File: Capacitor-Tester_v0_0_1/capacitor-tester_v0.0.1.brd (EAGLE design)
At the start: 100 x 80 mm, 32 parts, among them IC1 AD8531ARZ, IC2 MC34063EBD-TR, IC3 DAC6571IDBVT, IC5 AD8397ARDZ, J1 USB4125-GF-A-0190_REVA2, J2 DS1044-140G, J4 250-103, U1 AD5933, Y1 LFSPXO018034

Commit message: IN PROGRESS - arranging elements
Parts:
- added C3, C7: 100n, custom_library:C0603
- R15: value 5k-1% -> 10k-1%
- moved R15 345.0 mm to (59.6, 35.5), turned to 90 degrees
- moved L1 342.9 mm to (24.4, 26.1), flipped to the bottom, turned to 270 degrees
- moved R16 336.6 mm to (60.8, 22.1), turned to 270 degrees
- moved R6 330.2 mm to (56.8, 22.1), turned to 90 degrees
- moved R4 329.6 mm to (8.75, 33.1), turned to 270 degrees
- moved R5 329.1 mm to (58.8, 22.1), turned to 270 degrees
- moved R2 328.7 mm to (10.8, 32.9), turned to 90 degrees
- moved D2 319.7 mm to (7.25, 19.5), turned to 90 degrees
- moved IC1 319.1 mm to (8.00, 26.6), turned to 90 degrees
- moved IC5 318.6 mm to (59.0, 28.8), turned to 90 degrees
- moved C8 312.0 mm to (47.6, 32.2), turned to 270 degrees
- moved IC3 295.4 mm to (46.6, 38.1), turned to 90 degrees
- moved C6 247.8 mm to (16.5, 34.8), flipped to the bottom
- moved C5 244.0 mm to (36.0, 38.8), flipped to the bottom, turned to 90 degrees
- moved J4 242.9 mm to (15.8, 5.40)
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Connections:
- net +12V: now also C3.1; no longer D2.1
- net +5V: now also C7.1, D2.1
- net GND: now also C3.2, C7.2
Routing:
- net +5V: track 0.00 -> 128.6 mm, vias 0 -> 3
- net Z_OUT: track 0.00 -> 79.7 mm
- net SDA: track 0.00 -> 66.4 mm, vias 0 -> 1
- net +12V: track 0.00 -> 65.5 mm, vias 0 -> 2
- net SCL: track 0.00 -> 64.2 mm, vias 0 -> 1
- net VIN: track 0.00 -> 48.6 mm
- net UZA_OUT: track 0.00 -> 39.2 mm
- net VOUT: track 0.00 -> 38.4 mm
- net MCLK: track 0.00 -> 24.4 mm
- net FUNC_GEN: track 0.00 -> 20.4 mm
- net DAC_OUT: track 0.00 -> 18.9 mm, vias 0 -> 2
- net N$13: track 0.00 -> 17.1 mm
- net N$11: track 0.00 -> 15.7 mm
- net UZB_OUT: track 0.00 -> 11.7 mm
- net N$5: track 0.00 -> 10.3 mm
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- added copper zone on layer 1, net GND
- added copper zone on layer 16, net GND
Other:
- board size 100 x 80 mm -> 67 x 45 mm

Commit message: IN PROGRESS - arranging elements
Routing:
- net +5V: track 128.6 -> 0.00 mm
- net Z_OUT: track 79.7 -> 0.00 mm
- net SDA: track 66.4 -> 0.00 mm
- net +12V: track 65.5 -> 0.00 mm
- net SCL: track 64.2 -> 0.00 mm
- net VIN: track 48.6 -> 0.00 mm
- net UZA_OUT: track 39.2 -> 0.00 mm
- net VOUT: track 38.4 -> 0.00 mm
- net MCLK: track 24.4 -> 0.00 mm
- net FUNC_GEN: track 20.4 -> 0.00 mm
- net DAC_OUT: track 18.9 -> 0.00 mm
- net N$13: track 17.1 -> 0.00 mm
- net N$11: track 15.7 -> 0.00 mm
- net UZB_OUT: track 11.7 -> 0.00 mm
- net N$5: track 10.3 -> 0.00 mm
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
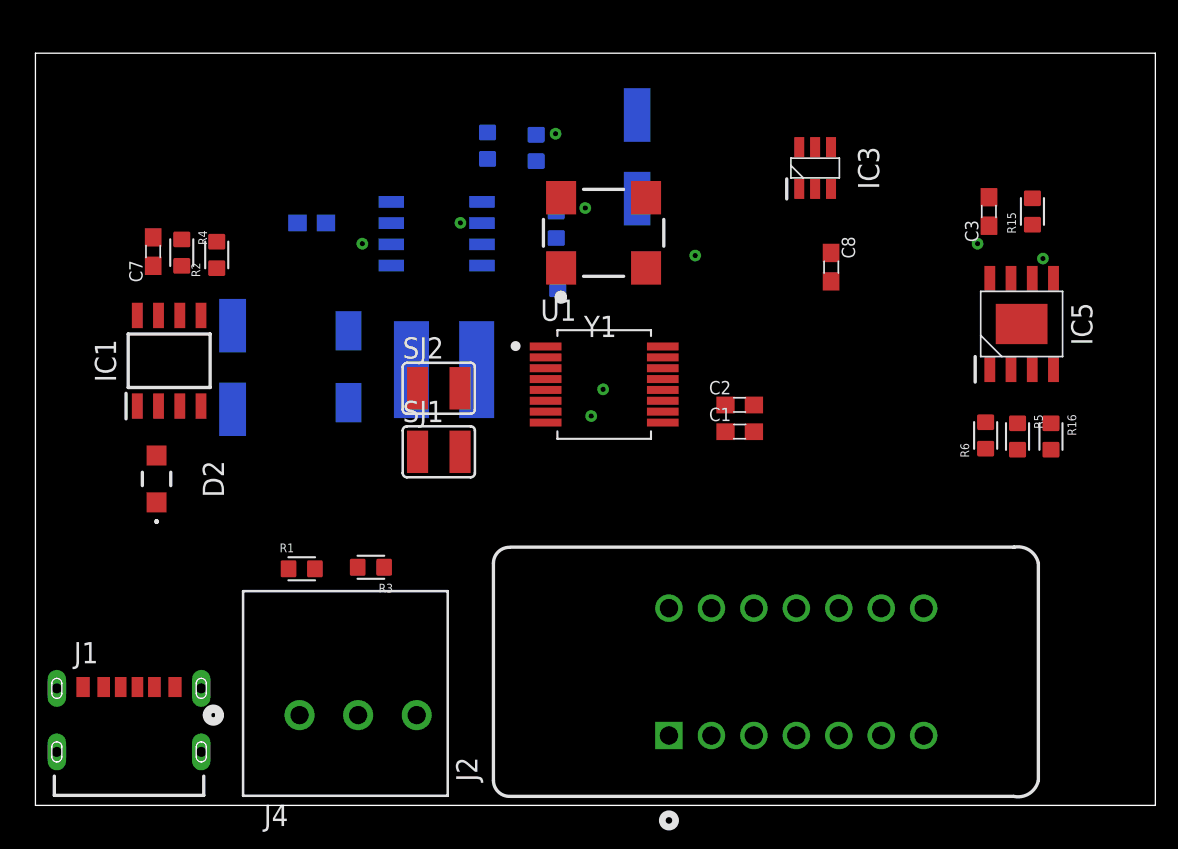
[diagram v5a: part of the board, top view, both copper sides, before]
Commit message: v0.0.1 - Routed traces
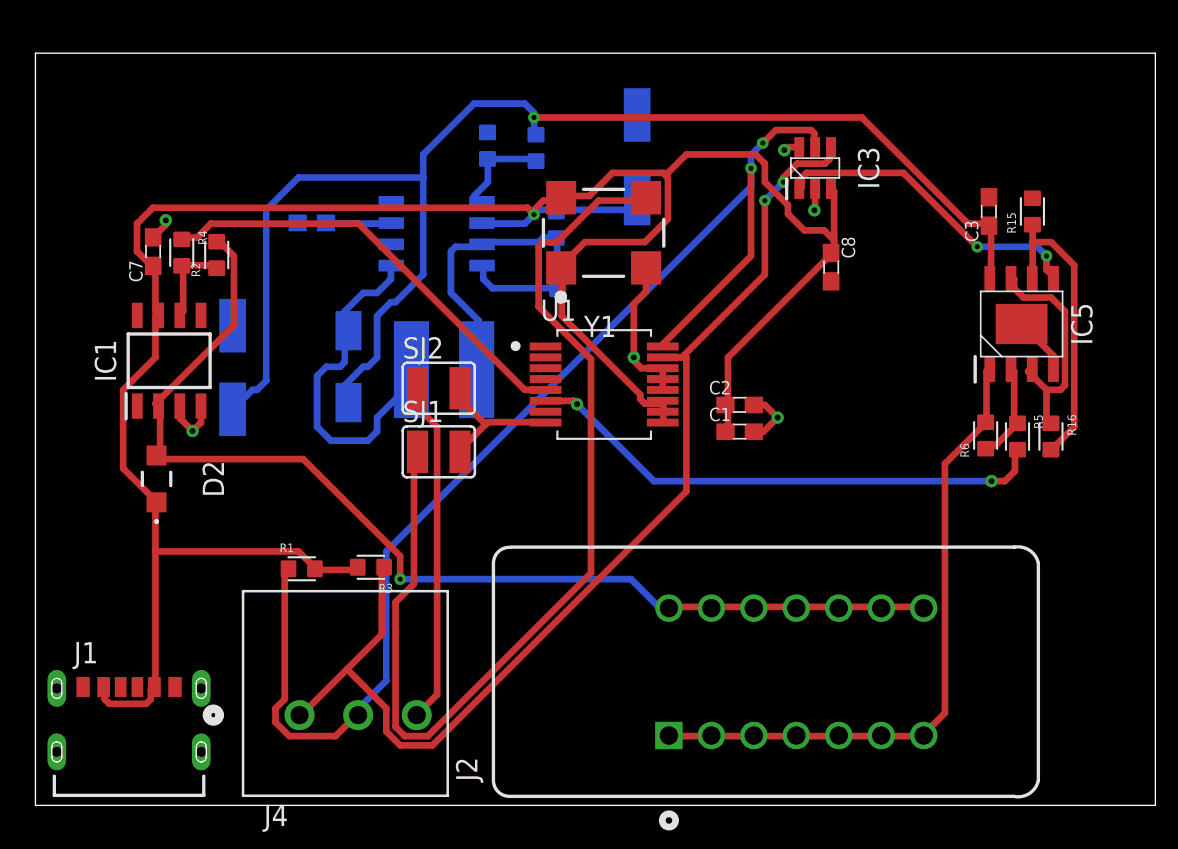
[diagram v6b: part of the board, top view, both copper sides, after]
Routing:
- net +5V: track 0.00 -> 144.9 mm, vias 3 -> 1
- net +12V: track 0.00 -> 82.9 mm, vias 2 -> 1
- net SCL: track 0.00 -> 76.8 mm, vias 1 -> 2
- net SDA: track 0.00 -> 66.9 mm, vias 1 -> 2
- net Z_OUT: track 0.00 -> 66.3 mm, vias 0 -> 1
- net MCLK: track 0.00 -> 61.5 mm
- net UZA_OUT: track 0.00 -> 38.9 mm
- net VOUT: track 0.00 -> 31.7 mm, vias 0 -> 2
- net VIN: track 0.00 -> 26.3 mm
- net GND: track 0.00 -> 23.2 mm, vias 0 -> 6
- net N$5: track 0.00 -> 21.4 mm
- net FUNC_GEN: track 0.00 -> 20.5 mm
- net DAC_OUT: track 0.00 -> 19.1 mm
- net N$13: track 0.00 -> 18.1 mm
- net N$11: track 0.00 -> 15.9 mm
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
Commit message: v0.0.1 - CMD renumber + tnames + bnames
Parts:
- removed IC5: AD8397ARDZ, AD8397ARDZ:SOIC127P600X175-9N
- removed J4: 250-103, custom_library:CONN3_250-103_WAG
- removed R15, R16: 10k-1%, custom_library:R0603
- added IC4: MC34063EBD-TR, MC34063EBD-TR:SOIC127P600X175-8N
- added J3: USB4125-GF-A-0190_REVA2, USB-C-6Pin:GCT_USB4125-GF-A-0190_REVA2
- added R7, R8: DNP-4k7-1%, custom_library:R0603
- C2: value 10u -> 100n
- C3: value 100n -> 10u
- C4: value 270u / 16V -> 10u; device EEEFKC271XSP:EEE0JA331XP -> custom_library:C0603
- C5: value 270u / 16V -> 100n; device EEEFKC271XSP:EEE0JA331XP -> custom_library:C0603
- C6: value 560p -> 270u / 16V; device custom_library:C0603 -> EEEFKC271XSP:EEE0JA331XP
- C7: value 100n -> 560p
- C8: value 10u -> 270u / 16V; device custom_library:C0603 -> EEEFKC271XSP:EEE0JA331XP
- D1: value SS14 -> PMEG6020ER,115; device SS14:DIOM5227X270N -> PMEG6020ER_115:PMEG6020ER115
- D2: value PMEG6020ER,115 -> SS14; device PMEG6020ER_115:PMEG6020ER115 -> SS14:DIOM5227X270N
- IC1: value AD8531ARZ -> DAC6571IDBVT; device AD8531ARZ:SOIC127P600X175-8N -> DAC6571IDBVT:SOT95P280X145-6N
- IC2: value MC34063EBD-TR -> AD8397ARDZ; device MC34063EBD-TR:SOIC127P600X175-8N -> AD8397ARDZ:SOIC127P600X175-9N
- IC3: value DAC6571IDBVT -> AD8531ARZ; device DAC6571IDBVT:SOT95P280X145-6N -> AD8531ARZ:SOIC127P600X175-8N
- J1: value USB4125-GF-A-0190_REVA2 -> DS1044-140G; device USB-C-6Pin:GCT_USB4125-GF-A-0190_REVA2 -> DS1044-140G:CONNFLY_DS1044-140G
- J2: value DS1044-140G -> 250-103; device DS1044-140G:CONNFLY_DS1044-140G -> custom_library:CONN3_250-103_WAG
- R1, R3: value DNP-4k7-1% -> 10k-1%
- R10: value 1k-1% -> R133-1%
- R11: value R133-1% -> 8k66-1%
- R12: value 180R-1% -> 1k-1%
- R2: value 10k-1% -> DNP-10k-1%
- R4: value DNP-10k-1% -> 1k-1%
- R6: value 1k-1% -> 10k-1%
- R9: value 8k66-1% -> 180R-1%
- moved R4 49.3 mm to (56.8, 22.1), turned to 90 degrees
- moved R1 48.7 mm to (59.6, 35.5), turned to 90 degrees
- moved IC1 40.3 mm to (46.6, 38.1)
- moved IC3 40.3 mm to (8.00, 26.6)
- moved J1 40.1 mm to (45.5, 7.99), turned to 90 degrees
- moved C2 36.3 mm to (7.05, 33.1), turned to 90 degrees
- moved IC2 35.4 mm to (59.0, 28.8), flipped to the top, turned to 90 degrees
- moved C4 30.4 mm to (42.1, 24.0), flipped to the top, turned to 0 degrees
- moved J2 29.8 mm to (15.8, 5.40), turned to 0 degrees
- moved R3 20.8 mm to (10.8, 32.9), turned to 90 degrees
- moved C1 19.9 mm to (57.0, 35.5), turned to 90 degrees
- moved C5 17.6 mm to (42.1, 22.4), flipped to the top, turned to 0 degrees
- moved C8 13.3 mm to (36.0, 38.8), flipped to the bottom, turned to 90 degrees
- moved D1 13.3 mm to (7.25, 19.5), flipped to the top
- moved D2 13.3 mm to (18.7, 26.2), flipped to the bottom
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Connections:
- net +12V: now also C1.1, C6.1, D2.1, IC2.8, R11.1; no longer C3.1, C4.1, D1.1, IC5.8, R9.1
- net +5V: now also C3.1, C4.1, D1.1, IC1.3, IC3.7, IC4.6, J3.A9, J3.B9, R10.1, R7.2, R8.2; no longer C1.1, C7.1, D2.1, IC1.7, IC2.6, IC3.3, J1.A9, J1.B9, R1.2, R11.1, R3.2
- net DAC_OUT: now also IC1.1, IC2.5; no longer IC3.1, IC5.5
- net FUNC_GEN: now also J2.3, SJ1.1; no longer J4.3, SJ2.1
- net GND: now also IC1.2, IC1.6, IC2.9, IC3.3, IC3.4, IC4.2, IC4.4, J3.A12, J3.B12, J3.S1, J3.S2, J3.S3, J3.S4, R1.2, R12.2; no longer IC1.3, IC1.4, IC2.2, IC3.2, IC3.6, IC5.4, IC5.9, J1.A12, J1.B12, J1.S1, J1.S2, J1.S3, J1.S4, R10.2, R15.2
- net MCLK: now also SJ2.1; no longer SJ1.1
- net N$1: now also IC3.6, R2.2, R3.1; no longer IC1.6, R2.1, R4.2
- net N$10: now also C7.1, IC4.3; no longer C6.1, IC2.3
- net N$11: now also IC4.7, R10.2, R9.2; no longer IC2.7, R11.2, R12.2
- net N$13: now also IC2.6, R1.1, R6.2; no longer IC5.6, R15.1, R16.2
- net N$4: now also IC2.2, R4.1; no longer IC5.2, R6.1
- net N$5: now also D2.2, IC4.1; no longer D1.2, IC2.1
- net N$7: now also IC4.5, R11.2, R12.1; no longer IC2.5, R10.1, R9.2
- net N$8: now also IC4.8, R9.1; no longer IC2.8, R12.1
- net SCL: now also IC1.5, J2.2, R8.1; no longer IC3.5, J4.2, R1.1
- net SDA: now also IC1.4, J2.1, R7.1; no longer IC3.4, J4.1, R3.1
- net UZA_OUT: now also IC2.1, J1.1, J1.2, J1.3, J1.4, J1.5, J1.6, J1.7, R4.2; no longer IC5.1, J2.1, J2.2, J2.3, J2.4, J2.5, J2.6, J2.7, R6.2
- net UZB_OUT: now also IC2.3, IC2.7, R6.1; no longer IC5.3, IC5.7, R16.1
- net VIN: now also R2.1; no longer R4.1
- net Z_OUT: now also D1.2, IC3.2, J1.10, J1.11, J1.12, J1.13, J1.14, J1.8, J1.9, R3.2; no longer D2.2, IC1.2, J2.10, J2.11, J2.12, J2.13, J2.14, J2.8, J2.9, R2.2
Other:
- board text added: "FUNC_GEN"
- board text added: "MCLK"

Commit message: v0.0.1 - Revert to commit b06d3d6
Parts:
- removed IC4: MC34063EBD-TR, MC34063EBD-TR:SOIC127P600X175-8N
- removed J3: USB4125-GF-A-0190_REVA2, USB-C-6Pin:GCT_USB4125-GF-A-0190_REVA2
- removed R7, R8: DNP-4k7-1%, custom_library:R0603
- added IC5: AD8397ARDZ, AD8397ARDZ:SOIC127P600X175-9N
- added J4: 250-103, custom_library:CONN3_250-103_WAG
- added R15, R16: 10k-1%, custom_library:R0603
- C2: value 100n -> 10u
- C3: value 10u -> 100n
- C4: value 10u -> 270u / 16V; device custom_library:C0603 -> EEEFKC271XSP:EEE0JA331XP
- C5: value 100n -> 270u / 16V; device custom_library:C0603 -> EEEFKC271XSP:EEE0JA331XP
- C6: value 270u / 16V -> 560p; device EEEFKC271XSP:EEE0JA331XP -> custom_library:C0603
- C7: value 560p -> 100n
- C8: value 270u / 16V -> 10u; device EEEFKC271XSP:EEE0JA331XP -> custom_library:C0603
- D1: value PMEG6020ER,115 -> SS14; device PMEG6020ER_115:PMEG6020ER115 -> SS14:DIOM5227X270N
- D2: value SS14 -> PMEG6020ER,115; device SS14:DIOM5227X270N -> PMEG6020ER_115:PMEG6020ER115
- IC1: value DAC6571IDBVT -> AD8531ARZ; device DAC6571IDBVT:SOT95P280X145-6N -> AD8531ARZ:SOIC127P600X175-8N
- IC2: value AD8397ARDZ -> MC34063EBD-TR; device AD8397ARDZ:SOIC127P600X175-9N -> MC34063EBD-TR:SOIC127P600X175-8N
- IC3: value AD8531ARZ -> DAC6571IDBVT; device AD8531ARZ:SOIC127P600X175-8N -> DAC6571IDBVT:SOT95P280X145-6N
- J1: value DS1044-140G -> USB4125-GF-A-0190_REVA2; device DS1044-140G:CONNFLY_DS1044-140G -> USB-C-6Pin:GCT_USB4125-GF-A-0190_REVA2
- J2: value 250-103 -> DS1044-140G; device custom_library:CONN3_250-103_WAG -> DS1044-140G:CONNFLY_DS1044-140G
- R1, R3: value 10k-1% -> DNP-4k7-1%
- R10: value R133-1% -> 1k-1%
- R11: value 8k66-1% -> R133-1%
- R12: value 1k-1% -> 180R-1%
- R2: value DNP-10k-1% -> 10k-1%
- R4: value 1k-1% -> DNP-10k-1%
- R6: value 10k-1% -> 1k-1%
- R9: value 180R-1% -> 8k66-1%
- moved R4 49.3 mm to (8.75, 33.1), turned to 270 degrees
- moved R1 48.7 mm to (15.9, 14.2), turned to 0 degrees
- moved IC1 40.3 mm to (8.00, 26.6)
- moved IC3 40.3 mm to (46.6, 38.1)
- moved J1 40.1 mm to (5.60, 4.00), turned to 0 degrees
- moved C2 36.3 mm to (42.1, 24.0), turned to 0 degrees
- moved IC2 35.4 mm to (24.0, 34.2), flipped to the bottom, turned to 180 degrees
- moved C4 30.4 mm to (11.8, 26.2), flipped to the bottom, turned to 90 degrees
- moved J2 29.8 mm to (45.5, 7.99), turned to 90 degrees
- moved R3 20.8 mm to (20.1, 14.2), turned to 180 degrees
- moved C1 19.9 mm to (42.1, 22.4), turned to 0 degrees
- moved C5 17.6 mm to (36.0, 38.8), flipped to the bottom, turned to 90 degrees
- moved C8 13.3 mm to (47.6, 32.2), flipped to the top, turned to 270 degrees
- moved D1 13.3 mm to (18.7, 26.2), flipped to the bottom
- moved D2 13.3 mm to (7.25, 19.5), flipped to the top
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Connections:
- net +12V: now also C3.1, C4.1, D1.1, IC5.8, R9.1; no longer C1.1, C6.1, D2.1, IC2.8, R11.1
- net +5V: now also C1.1, C7.1, D2.1, IC1.7, IC2.6, IC3.3, J1.A9, J1.B9, R1.2, R11.1, R3.2; no longer C3.1, C4.1, D1.1, IC1.3, IC3.7, IC4.6, J3.A9, J3.B9, R10.1, R7.2, R8.2
- net DAC_OUT: now also IC3.1, IC5.5; no longer IC1.1, IC2.5
- net FUNC_GEN: now also J4.3, SJ2.1; no longer J2.3, SJ1.1
- net GND: now also IC1.3, IC1.4, IC2.2, IC3.2, IC3.6, IC5.4, IC5.9, J1.A12, J1.B12, J1.S1, J1.S2, J1.S3, J1.S4, R10.2, R15.2; no longer IC1.2, IC1.6, IC2.9, IC3.3, IC3.4, IC4.2, IC4.4, J3.A12, J3.B12, J3.S1, J3.S2, J3.S3, J3.S4, R1.2, R12.2
- net MCLK: now also SJ1.1; no longer SJ2.1
- net N$1: now also IC1.6, R2.1, R4.2; no longer IC3.6, R2.2, R3.1
- net N$10: now also C6.1, IC2.3; no longer C7.1, IC4.3
- net N$11: now also IC2.7, R11.2, R12.2; no longer IC4.7, R10.2, R9.2
- net N$13: now also IC5.6, R15.1, R16.2; no longer IC2.6, R1.1, R6.2
- net N$4: now also IC5.2, R6.1; no longer IC2.2, R4.1
- net N$5: now also D1.2, IC2.1; no longer D2.2, IC4.1
- net N$7: now also IC2.5, R10.1, R9.2; no longer IC4.5, R11.2, R12.1
- net N$8: now also IC2.8, R12.1; no longer IC4.8, R9.1
- net SCL: now also IC3.5, J4.2, R1.1; no longer IC1.5, J2.2, R8.1
- net SDA: now also IC3.4, J4.1, R3.1; no longer IC1.4, J2.1, R7.1
- net UZA_OUT: now also IC5.1, J2.1, J2.2, J2.3, J2.4, J2.5, J2.6, J2.7, R6.2; no longer IC2.1, J1.1, J1.2, J1.3, J1.4, J1.5, J1.6, J1.7, R4.2
- net UZB_OUT: now also IC5.3, IC5.7, R16.1; no longer IC2.3, IC2.7, R6.1
- net VIN: now also R4.1; no longer R2.1
- net Z_OUT: now also D2.2, IC1.2, J2.10, J2.11, J2.12, J2.13, J2.14, J2.8, J2.9, R2.2; no longer D1.2, IC3.2, J1.10, J1.11, J1.12, J1.13, J1.14, J1.8, J1.9, R3.2
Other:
- board text removed: "FUNC_GEN"
- board text removed: "MCLK"
